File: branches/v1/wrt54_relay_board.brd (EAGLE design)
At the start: 90.5 x 87 mm, 62 parts, among them IC1 18F2550, IC2 786TV, IC3 MAX232, K1 351, K2 351, T1 2STX1360, T2 2STX1360, X1 C-GRID-05-70543

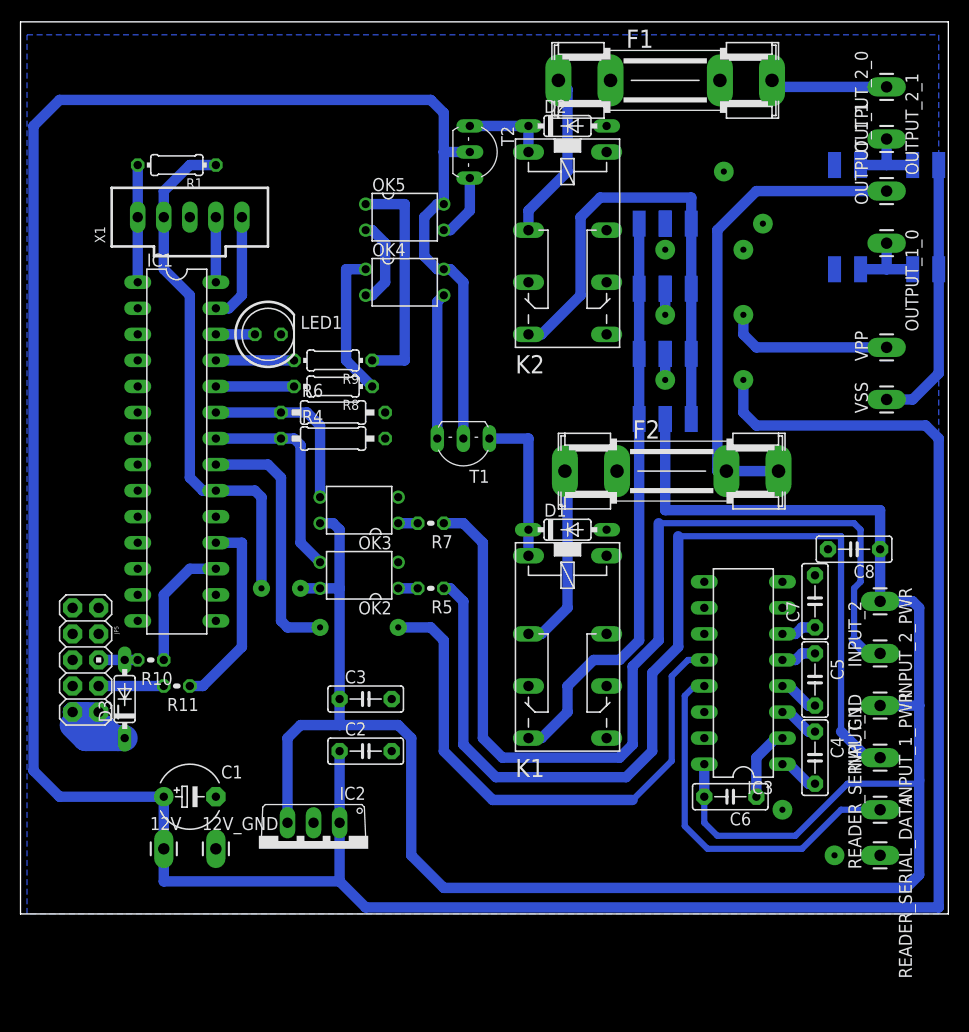
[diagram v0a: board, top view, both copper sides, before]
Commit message: smaller board layout
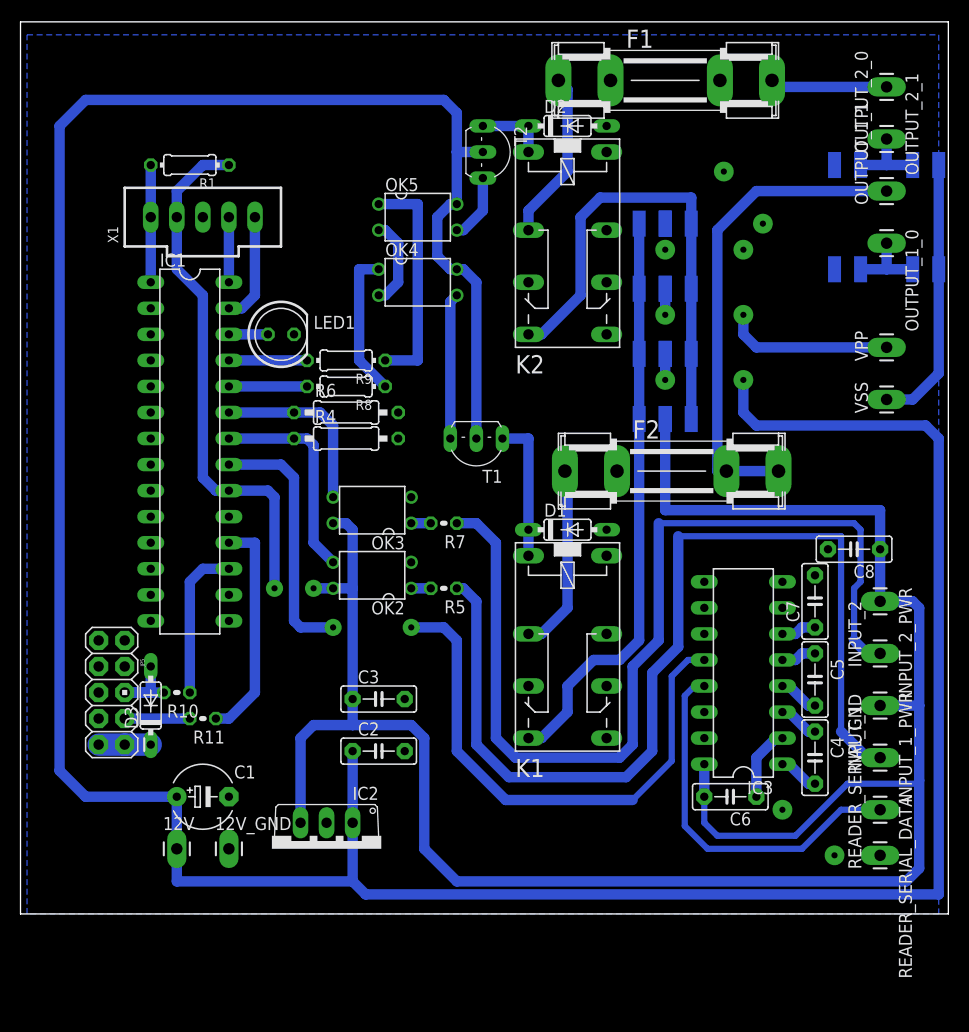
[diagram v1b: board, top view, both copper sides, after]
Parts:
- moved R11 4.07 mm to (15.2, 14.6)
- moved JP5 4.07 mm to (6.35, 17.1)
- moved R10 4.07 mm to (12.7, 17.1)
- moved D3 2.62 mm to (10.2, 15.9)
- moved OK4 1.27 mm to (36.2, 57.1)
- moved OK5 1.27 mm to (36.2, 63.5)
- moved T2 1.27 mm to (42.5, 69.8)
- moved IC1 1.27 mm to (14.0, 40.6)
- moved R1 1.27 mm to (14.0, 68.6)
- moved 12V 1.27 mm to (12.7, 1.91)
- moved 12V_GND 1.27 mm to (17.8, 1.91)
- moved C1 1.27 mm to (15.2, 6.99)
- moved C2 1.27 mm to (32.4, 11.4)
- moved C3 1.27 mm to (32.4, 16.5)
- moved IC2 1.27 mm to (27.3, 1.91)
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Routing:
- net N$33: track 14.5 -> 5.08 mm
- net +12V: track 325.1 -> 319.5 mm
- net N$34: track 3.81 -> 8.89 mm
- net N$25: track 19.4 -> 22.0 mm
- net N$24: track 12.5 -> 15.1 mm
- net +5V: track 266.2 -> 263.7 mm
- net N$5: track 95.0 -> 93.7 mm
- net N$3: track 99.0 -> 97.7 mm
- net N$15: track 78.5 -> 77.3 mm
- net N$12: track 15.2 -> 14.0 mm
- net N$11: track 8.26 -> 6.99 mm
